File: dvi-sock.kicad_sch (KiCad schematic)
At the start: 13 parts, among them J1 Conn_01x05, J2 Conn_01x05, J3 Conn_01x03, J4 NOT_HDMI_A, J5 2.54mm_2p_nofit

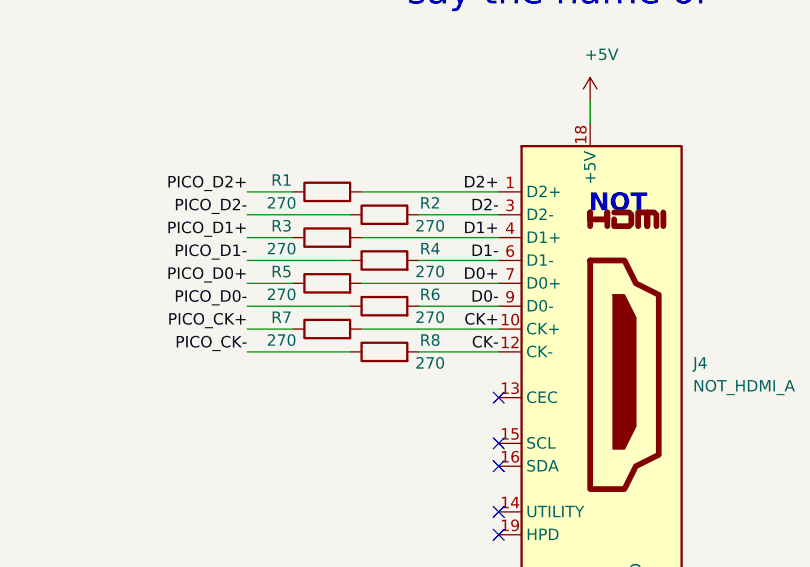
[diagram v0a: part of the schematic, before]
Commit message: Rev B: Use parts available for JLCPCB SMT assembly
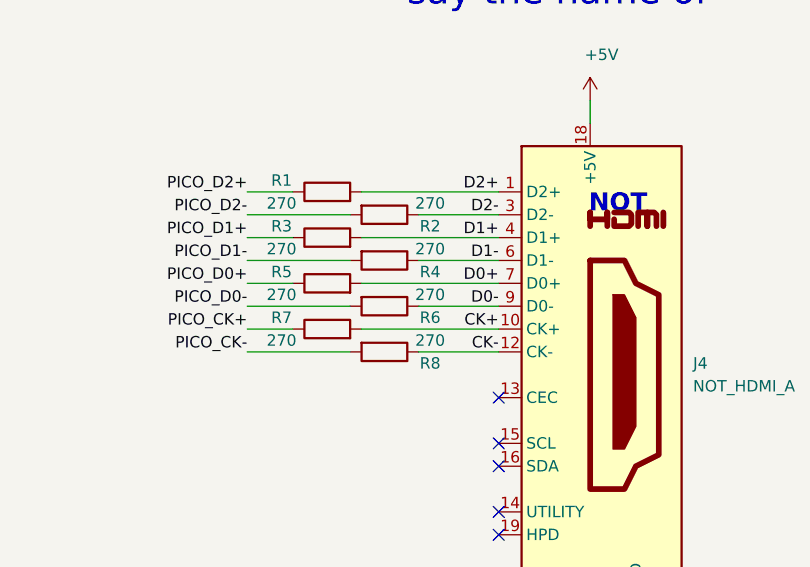
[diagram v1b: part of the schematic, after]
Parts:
- J4: footprint dvi-sock:HDMI-SS-53000 -> Connector_HDMI:HDMI_A_Molex_208658-1001_Horizontal; LCSC (none) -> C138388
- R1, R2, R3, R4, R5, R6, R7, R8: footprint Resistor_SMD:R_0402_1005Metric -> Resistor_SMD:R_0603_1608Metric; LCSC (none) -> C22966
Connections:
- net CK-: now also R8.1; no longer R8.2
- net D0-: now also R6.1; no longer R6.2
- net D1-: now also R4.1; no longer R4.2
- net D2-: now also R2.1; no longer R2.2
- net PICO_CK-: now also R8.2; no longer R8.1
- net PICO_D0-: now also R6.2; no longer R6.1
- net PICO_D1-: now also R4.2; no longer R4.1
- net PICO_D2-: now also R2.2; no longer R2.1
